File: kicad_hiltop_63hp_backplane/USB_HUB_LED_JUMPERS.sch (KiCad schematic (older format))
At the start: 86 parts, among them J4 4POS_JUMPER, J5 4POS_JUMPER, J6 4POS_JUMPER, J7 4POS_JUMPER, J8 4POS_JUMPER

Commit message: PCI EXPRESS 96
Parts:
- gave numbers to parts that had none: 64

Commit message: Added new PCB outline for the backplane
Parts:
- C1, C10, C11, C12, C13, C14, C15, C16, C17, C18, C2, C3, C4, C5, C6, C7, C8, C9: symbol device:C -> hiltop_backplane_brd-rescue:C-device
- D1: symbol ESD_Protection:NUP2105L -> hiltop_backplane_brd-rescue:NUP2105L-ESD_Protection
- D10, D11, D12, D13, D14, D15, D16, D17, D18, D19, D20, D21, D22, D23, D24, D25, D26, D27, D6, D7, D8, D9: symbol device:LED -> hiltop_backplane_brd-rescue:LED-device
- J10: symbol Connector1:USB_B_Micro -> hiltop_backplane_brd-rescue:USB_B_Micro-Connector1
- J4, J5, J6, J7, J8: symbol gti_Lattice:4POS_JUMPER -> hiltop_backplane_brd-rescue:4POS_JUMPER-gti_Lattice
- L6: symbol device:Ferrite_Bead -> hiltop_backplane_brd-rescue:Ferrite_Bead-device
- R1, R10, R11, R12, R13, R14, R147, R148, R149, R15, R150, R151, R152, R153, R154, R16, R17, R2, R3, R4, R5, R6, R60, R61, R62, R63, R64, R65, R7, R72, R73, R74, R8, R9: symbol device:R -> hiltop_backplane_brd-rescue:R-device
- TP2: symbol Connector1:Test_Point -> hiltop_backplane_brd-rescue:Test_Point-Connector1
- U1: symbol Devtank:USB2517 -> hiltop_backplane_brd-rescue:USB2517-Devtank
- Y2: symbol device:Crystal -> hiltop_backplane_brd-rescue:Crystal-device

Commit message: first pass draft for review
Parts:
- removed unit 2 of U1
- added U?: USB2517, MODULE, symbol Devtank:USB2517
- C1, C10, C11, C12, C13, C14, C15, C16, C17, C18, C2, C3, C4, C5, C6, C7, C8, C9: symbol hiltop_backplane_brd-rescue:C-device -> device:C
- D1: symbol hiltop_backplane_brd-rescue:NUP2105L-ESD_Protection -> ESD_Protection:NUP2105L
- D10, D11, D12, D13, D14, D15, D16, D17, D18, D19, D20, D21, D22, D23, D24, D25, D26, D27, D6, D7, D8, D9: symbol hiltop_backplane_brd-rescue:LED-device -> device:LED
- J10: symbol hiltop_backplane_brd-rescue:USB_B_Micro-Connector1 -> Connector:USB_B_Micro
- J4, J5, J6, J7, J8: symbol hiltop_backplane_brd-rescue:4POS_JUMPER-gti_Lattice -> gti_Lattice:4POS_JUMPER
- L6: symbol hiltop_backplane_brd-rescue:Ferrite_Bead-device -> device:Ferrite_Bead
- R1, R10, R11, R12, R13, R14, R147, R148, R149, R15, R150, R151, R152, R153, R154, R16, R17, R2, R3, R4, R5, R6, R60, R61, R62, R63, R64, R65, R7, R72, R73, R74, R8, R9: symbol hiltop_backplane_brd-rescue:R-device -> device:R
- TP2: symbol hiltop_backplane_brd-rescue:Test_Point-Connector1 -> Connector:TestPoint
- U1: symbol hiltop_backplane_brd-rescue:USB2517-Devtank -> Devtank:USB2517
- Y2: symbol hiltop_backplane_brd-rescue:Crystal-device -> device:Crystal
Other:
- note removed: "4.7V from USB"

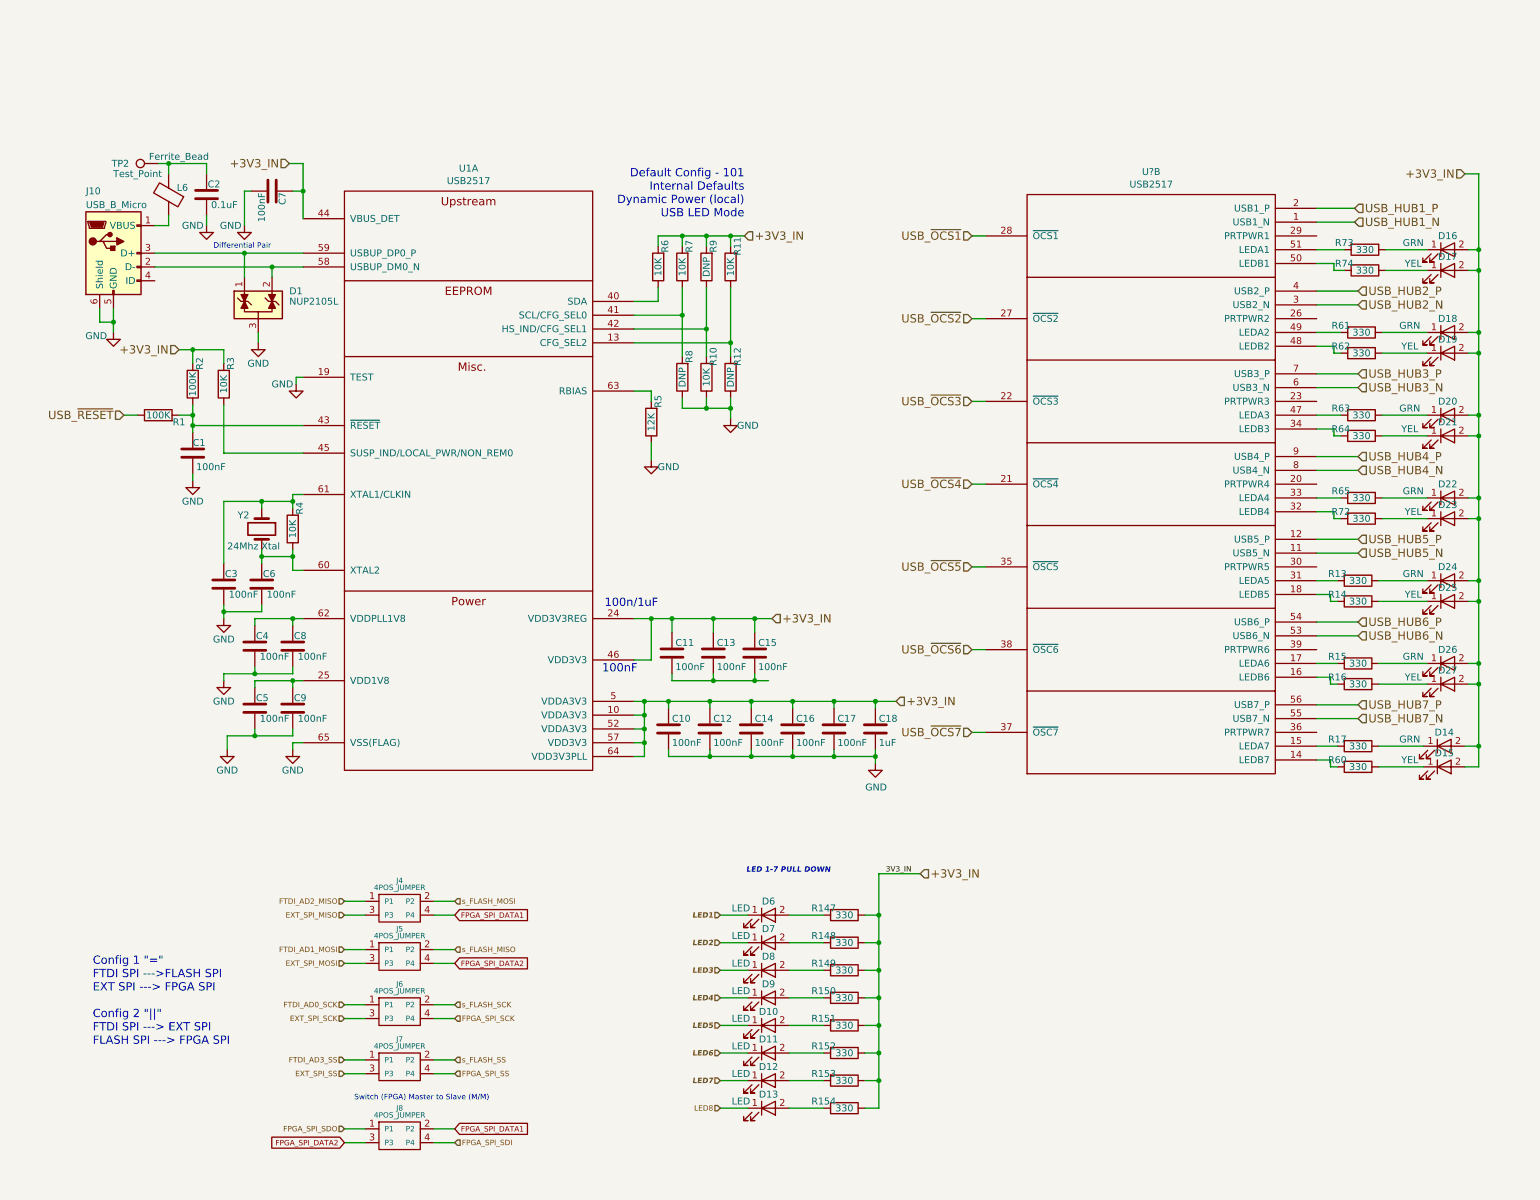
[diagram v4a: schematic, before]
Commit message: Schematic updated to reflect USB logic and Global nets changed to local nets, renamed signals in motherboard connector
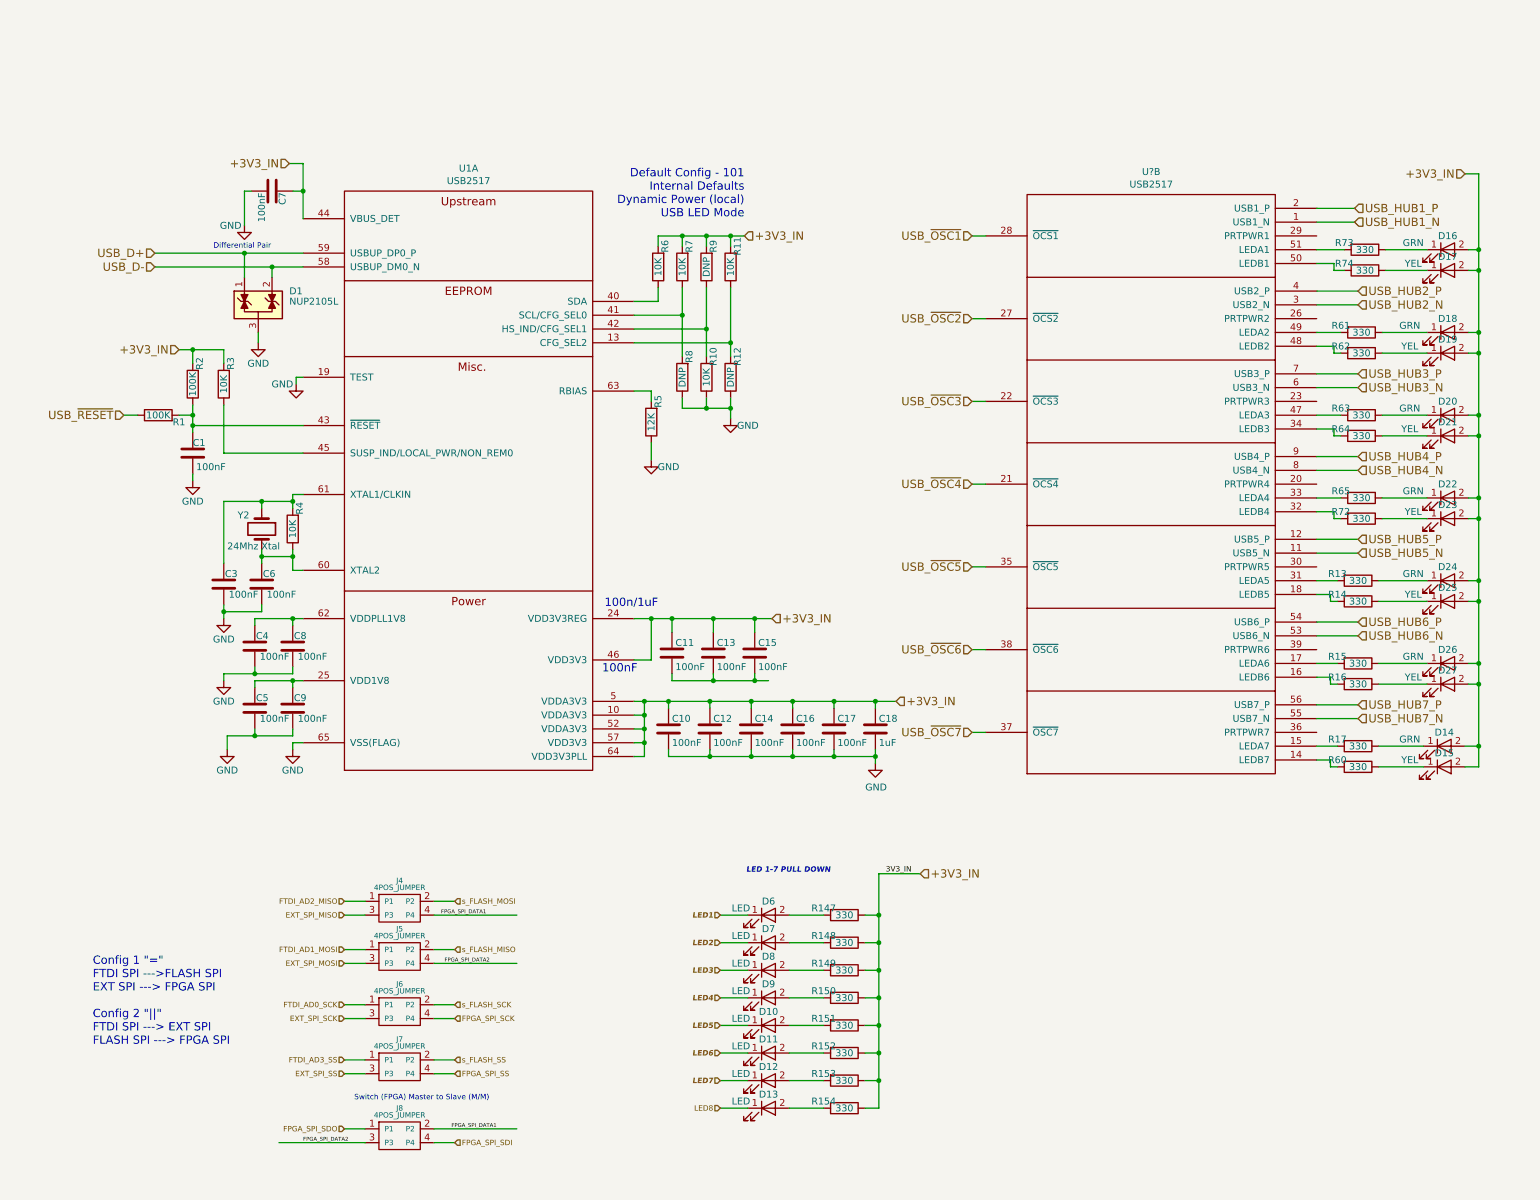
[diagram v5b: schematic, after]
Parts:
- removed C2: 0.1uF, Capacitor_SMD:C_0603_1608Metric, symbol device:C
- removed J10: USB_B_Micro, Connector_USB:USB_Micro-B_GCT_USB3076-30-A, symbol Connector:USB_B_Micro
- removed L6: Ferrite_Bead, Inductor_SMD:L_0603_1608Metric, symbol device:Ferrite_Bead
- removed TP2: Test_Point, TestPoint:TestPoint_Pad_D1.0mm, symbol Connector:TestPoint
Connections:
- net USB_D-: now reaches D1.2 (K), U1.58 (USBUP_DM0_N)
- net USB_D+: now reaches D1.1 (K), U1.59 (USBUP_DP0_P)
- net USB_~OCS1 renamed USB_~OSC1
- net USB_~OCS2 renamed USB_~OSC2
- net USB_~OCS3 renamed USB_~OSC3
- net USB_~OCS4 renamed USB_~OSC4
- net USB_~OCS5 renamed USB_~OSC5
- net USB_~OCS6 renamed USB_~OSC6
- net USB_~OCS7 renamed USB_~OSC7
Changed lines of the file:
@@
 $Descr A4 11693 8268
 encoding utf-8
-Sheet 3 6
+Sheet 6 6
 Title ""
 Date ""
@@
 	2700 6050 2850 6050
 Wire Wire Line
-	3350 6050 3500 6050
+	3350 6050 3950 6050
 Wire Wire Line
 	2700 6400 2850 6400
 Wire Wire Line
-	3350 6400 3500 6400
+	3350 6400 3950 6400
 Wire Wire Line
 	2700 6800 2850 6800
@@
 	2850 7600 2700 7600
 Wire Wire Line
-	3350 7600 3500 7600
+	3350 7600 3950 7600
 Wire Wire Line
 	3350 7700 3500 7700
 Wire Wire Line
-	2850 7700 2700 7700
+	2850 7700 2225 7700
 Text Notes 3750 7400 2    39   ~ 0
 Switch (FPGA) Master to Slave (M/M)\n
@@
 	5500 2450 5500 2375
 Connection ~ 5500 2375
-$Comp
-L Connector:USB_B_Micro J?
-U 1 1 5C68B09B
-P 1025 1250
-AR Path="/5A077B59/5C68B09B" Ref="J?"  Part="1"
-AR Path="/5A077C30/5C68B09B" Ref="J10"  Part="1"
-F 0 "J10" H 825 1700 50  0000 L CNN
-F 1 "USB_B_Micro" H 825 1600 50  0000 L CNN
-F 2 "Connector_USB:USB_Micro-B_GCT_USB3076-30-A" H 1175 1200 50  0001 C CNN
-F 3 "" H 1175 1200 50  0001 C CNN
-	1    1025 1250
-	1    0    0    -1
-$EndComp
-$Comp
-L device:C C?
-U 1 1 5C68B0A2
-P 1700 825
-AR Path="/5A077B59/5C68B0A2" Ref="C?"  Part="1"
-AR Path="/5A077C30/5C68B0A2" Ref="C2"  Part="1"
-F 0 "C2" H 1600 750 50  0000 L CNN
-F 1 "0.1uF" H 1475 900 50  0000 L CNN
-F 2 "Capacitor_SMD:C_0603_1608Metric" H 1738 675 50  0001 C CNN
-F 3 "" H 1700 825 50  0001 C CNN
-	1    1700 825
-	-1   0    0    1
-$EndComp
-$Comp
-L device:Ferrite_Bead L?
-U 1 1 5C68B0A9
-P 1425 825
-AR Path="/5A077B59/5C68B0A9" Ref="L?"  Part="1"
-AR Path="/5A077C30/5C68B0A9" Ref="L6"  Part="1"
-F 0 "L6" H 1325 775 50  0000 C CNN
-F 1 "Ferrite_Bead" H 1350 550 50  0000 C CNN
-F 2 "Inductor_SMD:L_0603_1608Metric" V 1355 825 50  0001 C CNN
-F 3 "" H 1425 825 50  0001 C CNN
-	1    1425 825
-	-1   0    0    1
-$EndComp
-$Comp
-L power:GND #PWR?
-U 1 1 5C68B0B0
-P 1700 1050
-AR Path="/5A077B59/5C68B0B0" Ref="#PWR?"  Part="1"
-AR Path="/5A077C30/5C68B0B0" Ref="#PWR05"  Part="1"
-F 0 "#PWR05" H 1700 800 50  0001 C CNN
-F 1 "GND" H 1600 1050 50  0000 C CNN
-F 2 "" H 1700 1050 50  0001 C CNN
-F 3 "" H 1700 1050 50  0001 C CNN
-	1    1700 1050
-	1    0    0    -1
-$EndComp
-$Comp
-L power:GND #PWR?
-U 1 1 5C68B0B6
-P 1025 1825
-AR Path="/5A077B59/5C68B0B6" Ref="#PWR?"  Part="1"
-AR Path="/5A077C30/5C68B0B6" Ref="#PWR03"  Part="1"
-F 0 "#PWR03" H 1025 1575 50  0001 C CNN
-F 1 "GND" H 900 1800 50  0000 C CNN
-F 2 "" H 1025 1825 50  0001 C CNN
-F 3 "" H 1025 1825 50  0001 C CNN
-	1    1025 1825
-	1    0    0    -1
-$EndComp
-$Comp
-L Connector:TestPoint TP?
-U 1 1 5C68B0D2
-P 1350 600
-AR Path="/5A077B59/5C68B0D2" Ref="TP?"  Part="1"
-AR Path="/5A077C30/5C68B0D2" Ref="TP2"  Part="1"
-F 0 "TP2" V 1350 875 50  0000 C CNN
-F 1 "Test_Point" V 1275 750 50  0000 C CNN
-F 2 "TestPoint:TestPoint_Pad_D1.0mm" H 1550 600 50  0001 C CNN
-F 3 "" H 1550 600 50  0001 C CNN
-	1    1350 600
-	0    -1   -1   0
-$EndComp
-Wire Wire Line
-	1025 1650 1025 1750
-Wire Wire Line
-	925  1650 925  1750
-Wire Wire Line
-	925  1750 1025 1750
-Connection ~ 1025 1750
-Wire Wire Line
-	1325 1050 1425 1050
-Wire Wire Line
-	1425 1050 1425 975
-Wire Wire Line
-	1700 975  1700 1050
 Text Notes 1750 1225 0    39   ~ 0
 Differential Pair
-Wire Wire Line
-	1025 1750 1025 1825
 $Comp
 L ESD_Protection:NUP2105L D?
@@
 Wire Wire Line
 	2075 1825 2075 1900
-Wire Wire Line
-	1350 600  1425 600
-Wire Wire Line
-	1425 600  1425 675
-Wire Wire Line
-	1425 600  1700 600
-Wire Wire Line
-	1700 600  1700 675
-Connection ~ 1425 600
 Wire Wire Line
 	1325 1250 1975 1250
@@
 	2325 4800 2325 4850
 Text HLabel 7250 1125 0    60   Input ~ 0
-USB_~OCS1
+USB_~OSC1
 Text HLabel 7250 1725 0    60   Input ~ 0
-USB_~OCS2
+USB_~OSC2
 Text HLabel 7250 2325 0    60   Input ~ 0
-USB_~OCS3
+USB_~OSC3
 Text HLabel 7250 2925 0    60   Input ~ 0
-USB_~OCS4
+USB_~OSC4
 Text HLabel 7250 3525 0    60   Input ~ 0
-USB_~OCS5
+USB_~OSC5
 Text HLabel 7250 4125 0    60   Input ~ 0
-USB_~OCS6
+USB_~OSC6
 Text HLabel 7250 4725 0    60   Input ~ 0
-USB_~OCS7
+USB_~OSC7
 Wire Wire Line
 	7250 4725 7350 4725
@@
 Wire Wire Line
 	10925 675  10925 1225
-Text GLabel 3500 6050 2    39   Input ~ 0
-FPGA_SPI_DATA1
-Text GLabel 3500 6400 2    39   Input ~ 0
-FPGA_SPI_DATA2
-Text GLabel 3500 7600 2    39   Input ~ 0
-FPGA_SPI_DATA1
-Text GLabel 2700 7700 0    39   Input ~ 0
-FPGA_SPI_DATA2
 Text HLabel 6875 5750 2    60   Input ~ 0
 +3V3_IN
@@
 	1    0    0    -1
 $EndComp
+Text HLabel 1325 1250 0    60   Input ~ 0
+USB_D+
+Text HLabel 1325 1350 0    60   Input ~ 0
+USB_D-
+Text Label 3400 6050 0    28   ~ 0
+FPGA_SPI_DATA1
+Text Label 3475 7600 0    28   ~ 0
+FPGA_SPI_DATA1
+Text Label 2400 7700 0    28   ~ 0
+FPGA_SPI_DATA2
+Text Label 3425 6400 0    28   ~ 0
+FPGA_SPI_DATA2
 $EndSCHEMATC

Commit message: lables connected to end of net, each component mapped to footprint, working on reducing error
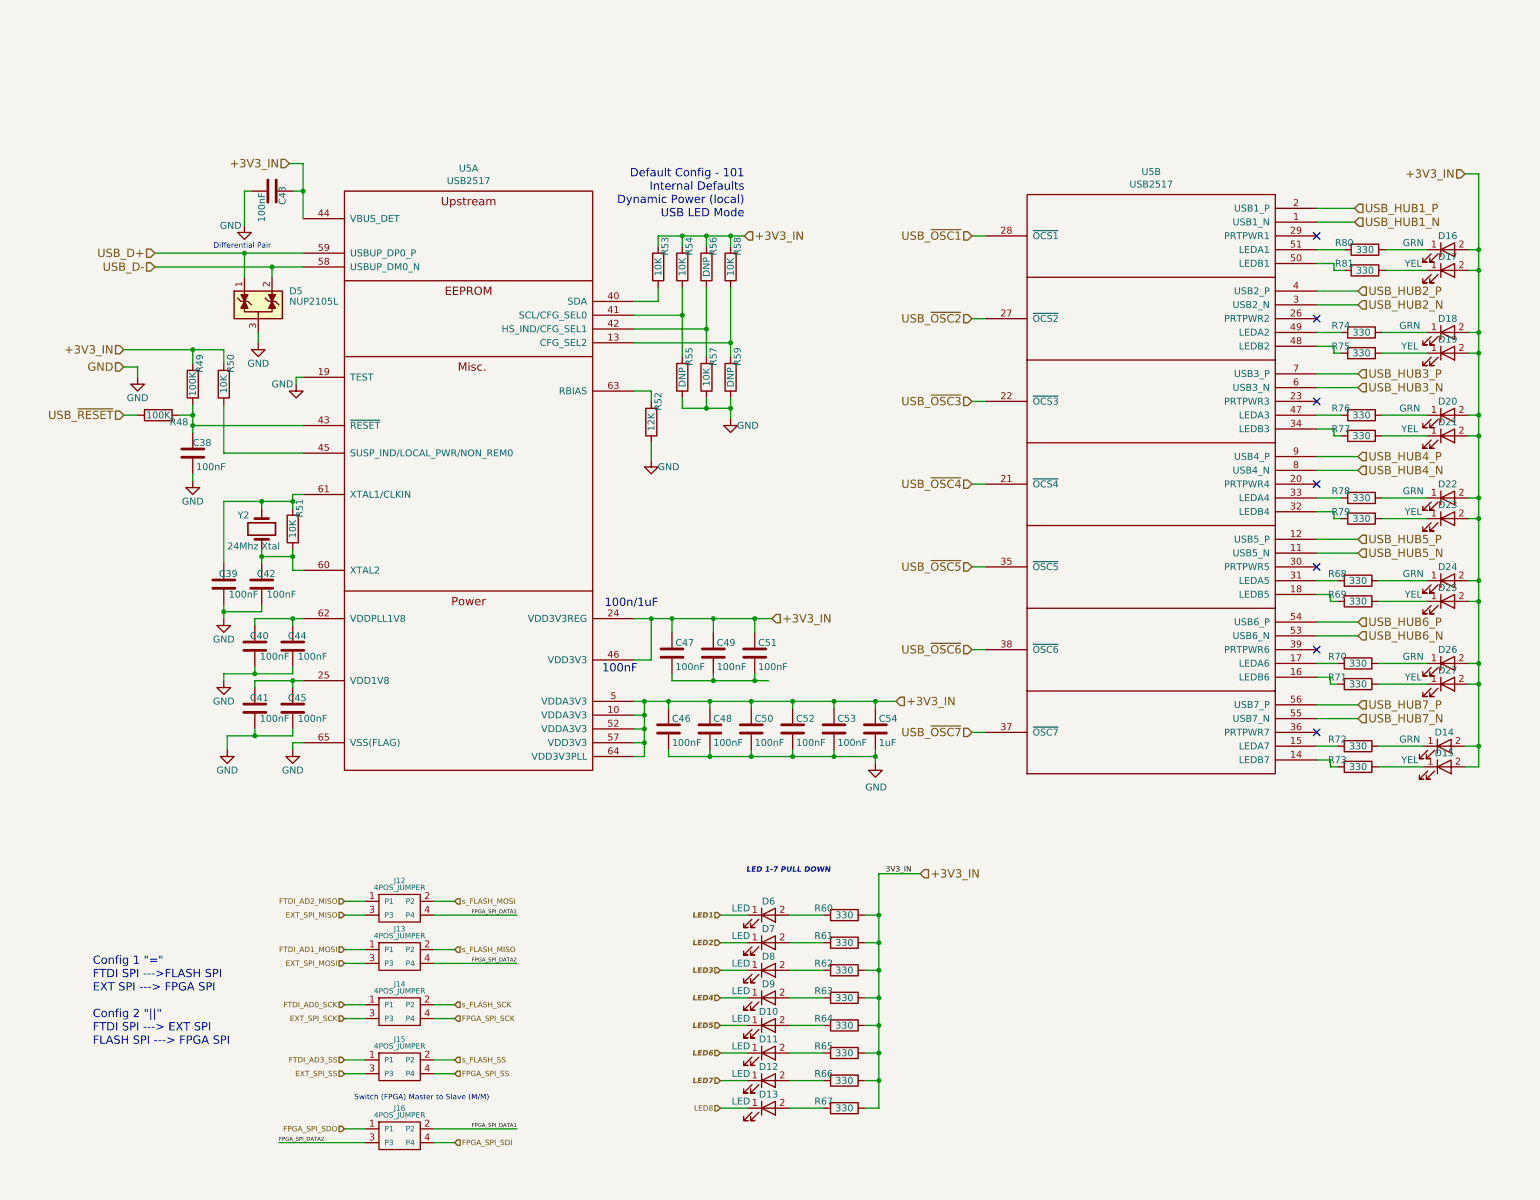
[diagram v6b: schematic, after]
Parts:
- Y2: footprint (none) -> Crystal:Crystal_SMD_7050-2Pin_7.0x5.0mm
- gave numbers to parts that had none: 1
- renumbered C1 to C38, C3 to C39, C4 to C40, C5 to C41, C6 to C42, C7 to C43, C8 to C44, C9 to C45, C10 to C46, C11 to C47, C12 to C48, C13 to C49, C14 to C50, C15 to C51, C16 to C52, C17 to C53, C18 to C54, D1 to D5, J4 to J12, J5 to J13, J6 to J14, J7 to J15, J8 to J16, R1 to R48, R2 to R49, R3 to R50, R4 to R51, R5 to R52, R6 to R53, R7 to R54, R8 to R55, R9 to R56, R10 to R57, R11 to R58, R12 to R59, R147 to R60, R148 to R61, R149 to R62, R150 to R63, R151 to R64, R152 to R65, R153 to R66, R154 to R67, R13 to R68, R14 to R69, R15 to R70, R16 to R71, R17 to R72, R60 to R73, R61 to R74, R62 to R75, R63 to R76, R64 to R77, R65 to R78, R72 to R79, R73 to R80, R74 to R81, U1 to U5
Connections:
- no-connect marks 0 -> 7

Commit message: schematic error reduced and footprint mapped
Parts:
- U5: footprint MODULE -> Package_DFN_QFN:QFN-64-1EP_9x9mm_P0.5mm_EP4.7x4.7mm
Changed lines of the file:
@@
 F 0 "U5" H 3600 4665 50  0000 C CNN
 F 1 "USB2517" H 3600 4574 50  0000 C CNN
-F 2 "MODULE" H 4350 25  50  0001 C CNN
+F 2 "Package_DFN_QFN:QFN-64-1EP_9x9mm_P0.5mm_EP4.7x4.7mm" H 4350 25  50  0001 C CNN
 F 3 "DOCUMENTATION" H 4200 125 50  0001 C CNN
 	1    3600 2650
@@
 F 0 "U5" H 8550 4690 50  0000 C CNN
 F 1 "USB2517" H 8550 4599 50  0000 C CNN
-F 2 "MODULE" H 9300 50  50  0001 C CNN
+F 2 "Package_DFN_QFN:QFN-64-1EP_9x9mm_P0.5mm_EP4.7x4.7mm" H 9300 50  50  0001 C CNN
 F 3 "DOCUMENTATION" H 9150 150 50  0001 C CNN
 	2    8550 2675

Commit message: first pass schematic placement
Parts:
- C49: value 100nF -> 1uF
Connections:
- net GND: now also C47.1, C49.1, C51.1
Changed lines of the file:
@@
 $Descr A4 11693 8268
 encoding utf-8
-Sheet 6 6
+Sheet 5 6
 Title ""
 Date ""
@@
 P 5375 4150
 F 0 "C49" H 5350 4075 50  0000 R CNN
-F 1 "100nF" H 5350 4250 50  0000 R CNN
+F 1 "1uF" H 5350 4250 50  0000 R CNN
 F 2 "Capacitor_SMD:C_0603_1608Metric" H 5413 4000 50  0001 C CNN
 F 3 "" H 5375 4150 50  0001 C CNN
@@
 AR Path="/5A077B59/5CBF7F97" Ref="C?"  Part="1"
 AR Path="/5A077C30/5CBF7F97" Ref="C40"  Part="1"
-F 0 "C40" H 1950 4025 50  0000 L CNN
+F 0 "C40" H 1900 4025 50  0000 L CNN
 F 1 "100nF" H 1800 4175 50  0000 L CNN
 F 2 "Capacitor_SMD:C_0603_1608Metric" H 2088 3950 50  0001 C CNN
@@
 AR Path="/5A077B59/5CBF8081" Ref="C?"  Part="1"
 AR Path="/5A077C30/5CBF8081" Ref="C44"  Part="1"
-F 0 "C44" H 2225 4025 50  0000 L CNN
+F 0 "C44" H 2175 4025 50  0000 L CNN
 F 1 "100nF" H 2075 4175 50  0000 L CNN
 F 2 "Capacitor_SMD:C_0603_1608Metric" H 2363 3950 50  0001 C CNN
@@
 AR Path="/5A077B59/5CBF82F9" Ref="C?"  Part="1"
 AR Path="/5A077C30/5CBF82F9" Ref="C41"  Part="1"
-F 0 "C41" H 1950 4475 50  0000 L CNN
+F 0 "C41" H 1900 4475 50  0000 L CNN
 F 1 "100nF" H 1800 4625 50  0000 L CNN
 F 2 "Capacitor_SMD:C_0603_1608Metric" H 2088 4400 50  0001 C CNN
@@
 AR Path="/5A077B59/5CBF83E1" Ref="C?"  Part="1"
 AR Path="/5A077C30/5CBF83E1" Ref="C45"  Part="1"
-F 0 "C45" H 2225 4475 50  0000 L CNN
+F 0 "C45" H 2175 4475 50  0000 L CNN
 F 1 "100nF" H 2075 4625 50  0000 L CNN
 F 2 "Capacitor_SMD:C_0603_1608Metric" H 2363 4400 50  0001 C CNN
@@
 NoConn ~ 9750 4125
 NoConn ~ 9750 4725
+$Comp
+L power:GND #PWR?
+U 1 1 5C67A6C1
+P 5775 4350
+F 0 "#PWR?" H 5775 4100 50  0001 C CNN
+F 1 "GND" H 5780 4177 50  0000 C CNN
+F 2 "" H 5775 4350 50  0001 C CNN
+F 3 "" H 5775 4350 50  0001 C CNN
+	1    5775 4350
+	1    0    0    -1
+$EndComp
 $EndSCHEMATC
